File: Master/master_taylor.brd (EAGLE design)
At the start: 74.4 x 74.4 mm, 50 parts, among them J1 ISP, K1 653002114822, K2 653002114822, K3 653002114822, K4 653002114822, U1 ATMEGA128RFA1, U2 TPS73633-DBVT, U3 ULN2003ADR, Y1 16MHz, Y2 32.768kHz

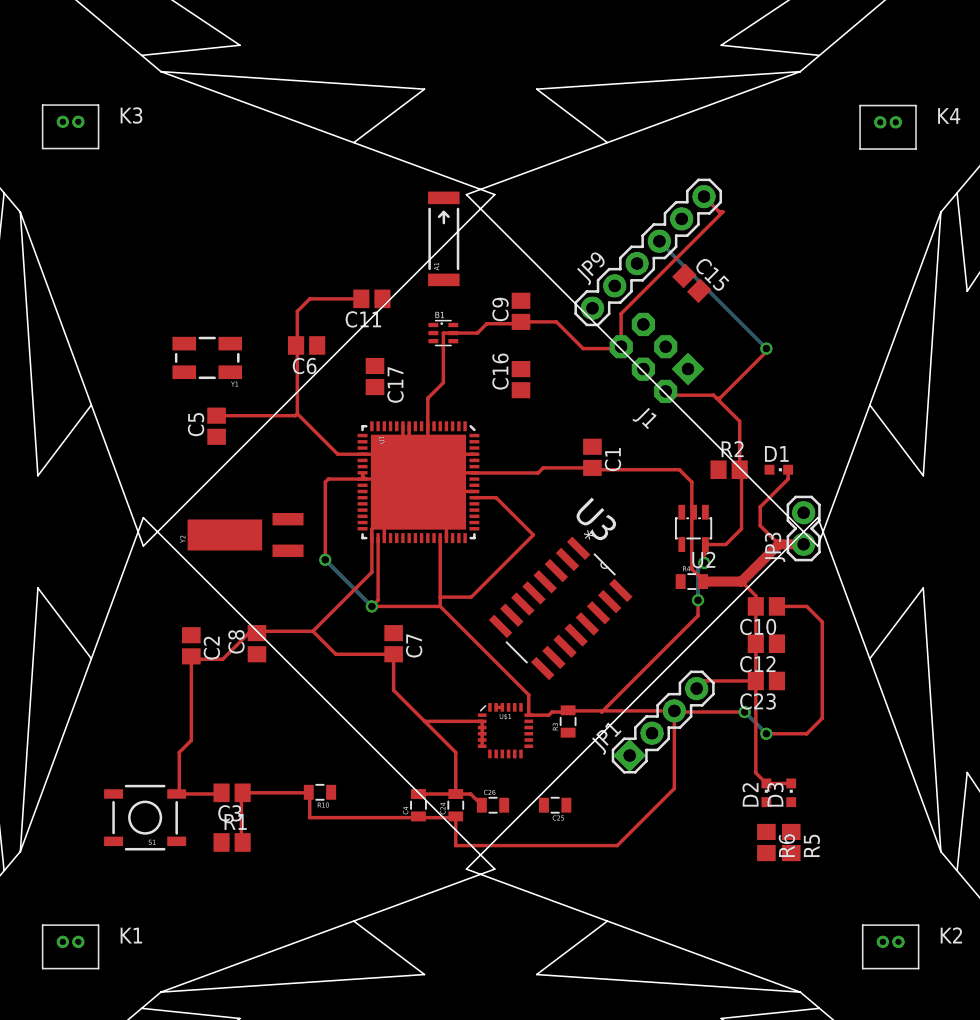
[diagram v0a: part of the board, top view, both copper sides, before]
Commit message: Routed most of VBAT, GND, and 3.3V
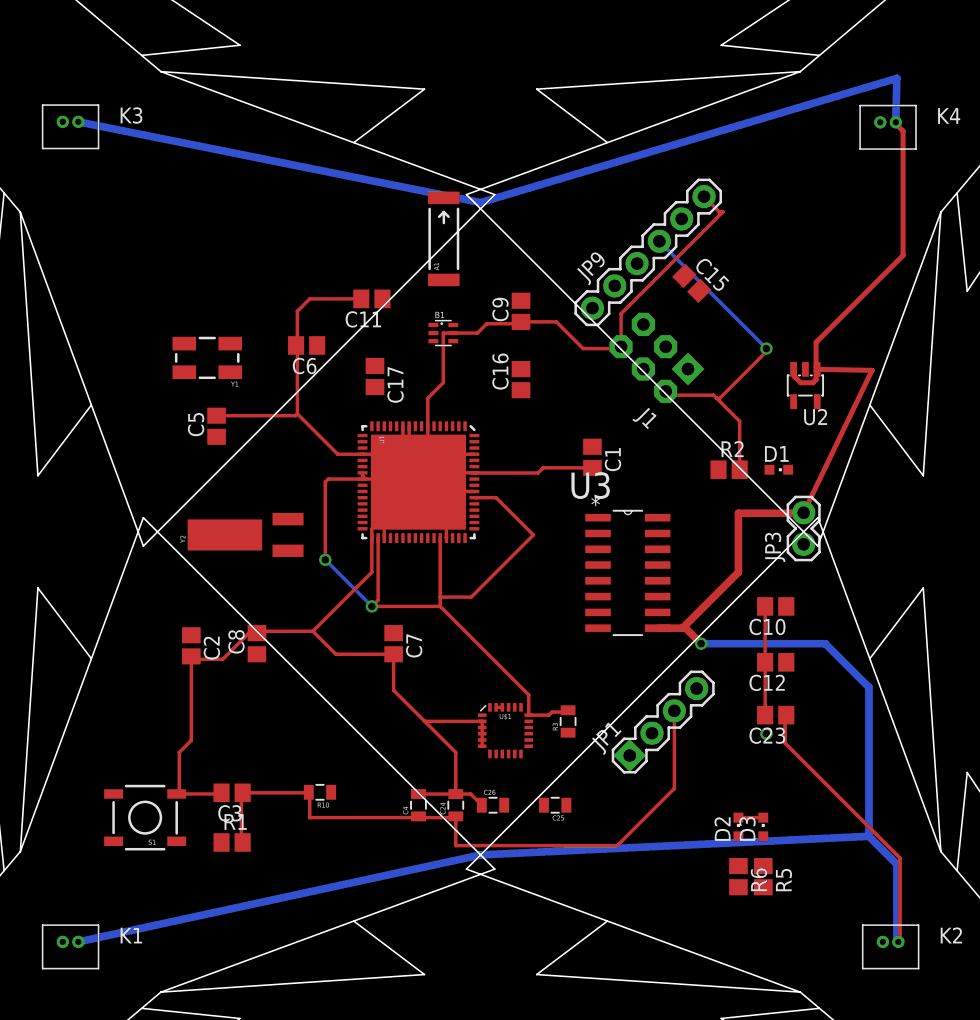
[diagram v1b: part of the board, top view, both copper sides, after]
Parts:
- removed R4: 0, SparkFun-Passives:0805
- moved U2 14.6 mm to (26.1, 11.8)
- moved U3 9.80 mm to (14.2, -7.75), turned to 0 degrees
- moved D2 3.55 mm to (20.8, -23.8)
- moved D3 3.55 mm to (22.8, -23.8)
- moved R5 3.55 mm to (22.8, -27.8)
- moved R6 3.55 mm to (20.8, -27.8)
- moved C23 2.85 mm to (23.8, -14.8)
- moved C12 1.68 mm to (23.8, -10.5)
- moved C10 0.75 mm to (23.8, -6.00)
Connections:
- removed net MAN_GND: R4.1, U3.5, U3.6, U3.7, U3.8
- net GND: now also U3.5, U3.6, U3.7, U3.8; no longer R4.2
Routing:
- net VBAT: track 0.00 -> 258.7 mm, vias 0 -> 1
- net 3.3V: track 202.5 -> 144.0 mm, vias 7 -> 4
- net GND: track 236.3 -> 189.9 mm

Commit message: Routing...
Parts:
- moved C7 7.25 mm to (-14.2, -9.00)
- moved U$1 3.26 mm to (-1.25, -16.2)
- moved U1 3.26 mm to (-3.25, 1.25), turned to 315 degrees
- moved C17 2.00 mm to (-8.50, 14.5)
- moved R3 1.89 mm to (5.21, -15.7), turned to 270 degrees
- moved JP1 1.58 mm to (10.5, -17.5)
- moved Y1 1.50 mm to (-23.5, 14.0)
- moved C26 1.35 mm to (2.25, -22.5)
- moved C6 1.27 mm to (-15.2, 14.8)
- moved C25 0.71 mm to (6.50, -22.5)
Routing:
- net GND: track 189.9 -> 242.4 mm
- net VBAT: track 258.7 -> 239.9 mm
- net SDA: track 0.00 -> 13.6 mm
- net 3.3V: track 144.0 -> 131.3 mm, vias 4 -> 5
- net RFANT: track 0.00 -> 10.9 mm
- net RESET: track 0.00 -> 9.29 mm
- net PE3: track 0.00 -> 8.71 mm
- net N$4: track 0.00 -> 8.51 mm
- net PE4: track 0.00 -> 7.94 mm
- net N$5: track 0.00 -> 7.15 mm
- net N$3: track 0.00 -> 7.05 mm
- net N$6: track 0.00 -> 6.56 mm
- net N$10: track 0.00 -> 6.45 mm, vias 0 -> 2
- net N$23: track 0.00 -> 5.43 mm
- net N$11: track 0.00 -> 4.78 mm
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
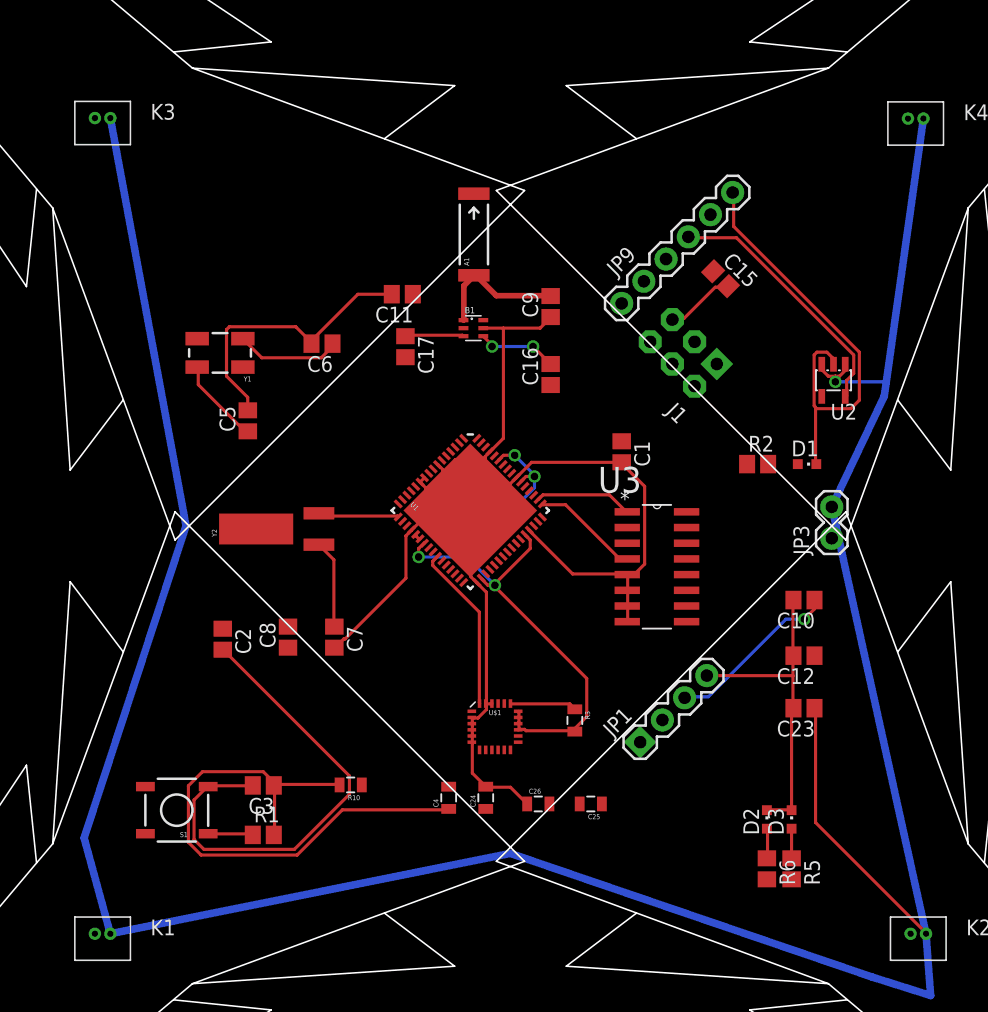
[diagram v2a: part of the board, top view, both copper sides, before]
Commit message: Routing is almost there...
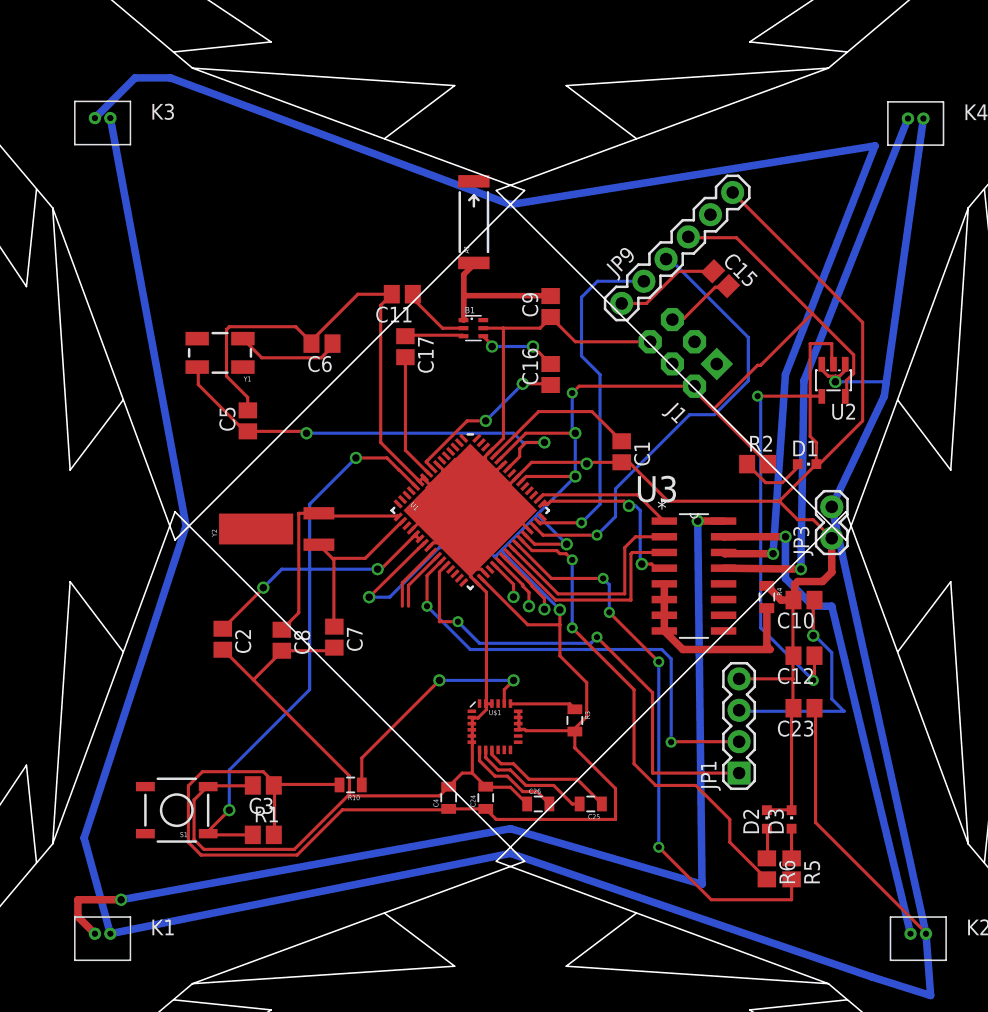
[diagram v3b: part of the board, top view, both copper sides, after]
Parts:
- added R4: 0, SparkFun-Passives:0805
- moved JP1 8.38 mm to (18.5, -20.0), turned to 90 degrees
- moved U3 3.09 mm to (17.2, -8.50)
- moved A1 1.00 mm to (-2.96, 24.6)
- moved C8 0.56 mm to (-18.5, -9.25), turned to 270 degrees
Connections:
- new net N$12: R4.2, U3.5, U3.6, U3.7, U3.8
- net GND: now also R4.1; no longer U3.5, U3.6, U3.7, U3.8
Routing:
- net N$31: track 0.00 -> 105.1 mm, vias 0 -> 1
- net 3.3V: track 131.3 -> 223.4 mm, vias 5 -> 7
- net N$29: track 0.00 -> 86.5 mm, vias 0 -> 2
- net GND: track 242.4 -> 304.4 mm, vias 0 -> 1
- net PB6: track 0.00 -> 46.0 mm, vias 0 -> 4
- net N$32: track 0.00 -> 44.3 mm, vias 0 -> 1
- net RESET: track 9.29 -> 50.4 mm, vias 0 -> 2
- net N$30: track 0.00 -> 40.3 mm, vias 0 -> 1
- net PB7: track 0.00 -> 39.2 mm, vias 0 -> 2
- net TX1: track 0.00 -> 38.4 mm, vias 0 -> 2
- net RX1: track 0.00 -> 38.0 mm, vias 0 -> 2
- net RX0: track 0.00 -> 37.0 mm, vias 0 -> 1
- net N$1: track 0.00 -> 32.1 mm, vias 0 -> 2
- net TX0: track 0.00 -> 28.6 mm, vias 0 -> 1
- net N$3: track 7.05 -> 35.7 mm, vias 0 -> 2
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
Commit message: Board all routed
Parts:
- moved C23 0.75 mm to (23.8, -15.5)
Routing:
- net MOSI: track 4.70 -> 50.2 mm, vias 1 -> 6
- net SCK: track 3.22 -> 43.9 mm, vias 1 -> 6
- net MISO: track 5.67 -> 40.5 mm, vias 1 -> 4
- net RESET: track 50.4 -> 80.4 mm, vias 2 -> 6
- net N$4: track 8.51 -> 38.0 mm, vias 0 -> 2
- net 3.3V: track 223.4 -> 252.4 mm, vias 7 -> 9
- net SCL: track 5.42 -> 18.3 mm, vias 0 -> 2
- net SDA: track 5.01 -> 16.8 mm, vias 0 -> 2
- net VBAT: track 239.9 -> 251.6 mm, vias 1 -> 3
- net GND: track 304.4 -> 305.7 mm
- net N$1: track 32.1 -> 31.3 mm
